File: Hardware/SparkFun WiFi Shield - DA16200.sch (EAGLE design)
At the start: 27 parts, among them J1 CORTEX_JTAG_DEBUG, U1 DA16200MOD-AAC4WA32

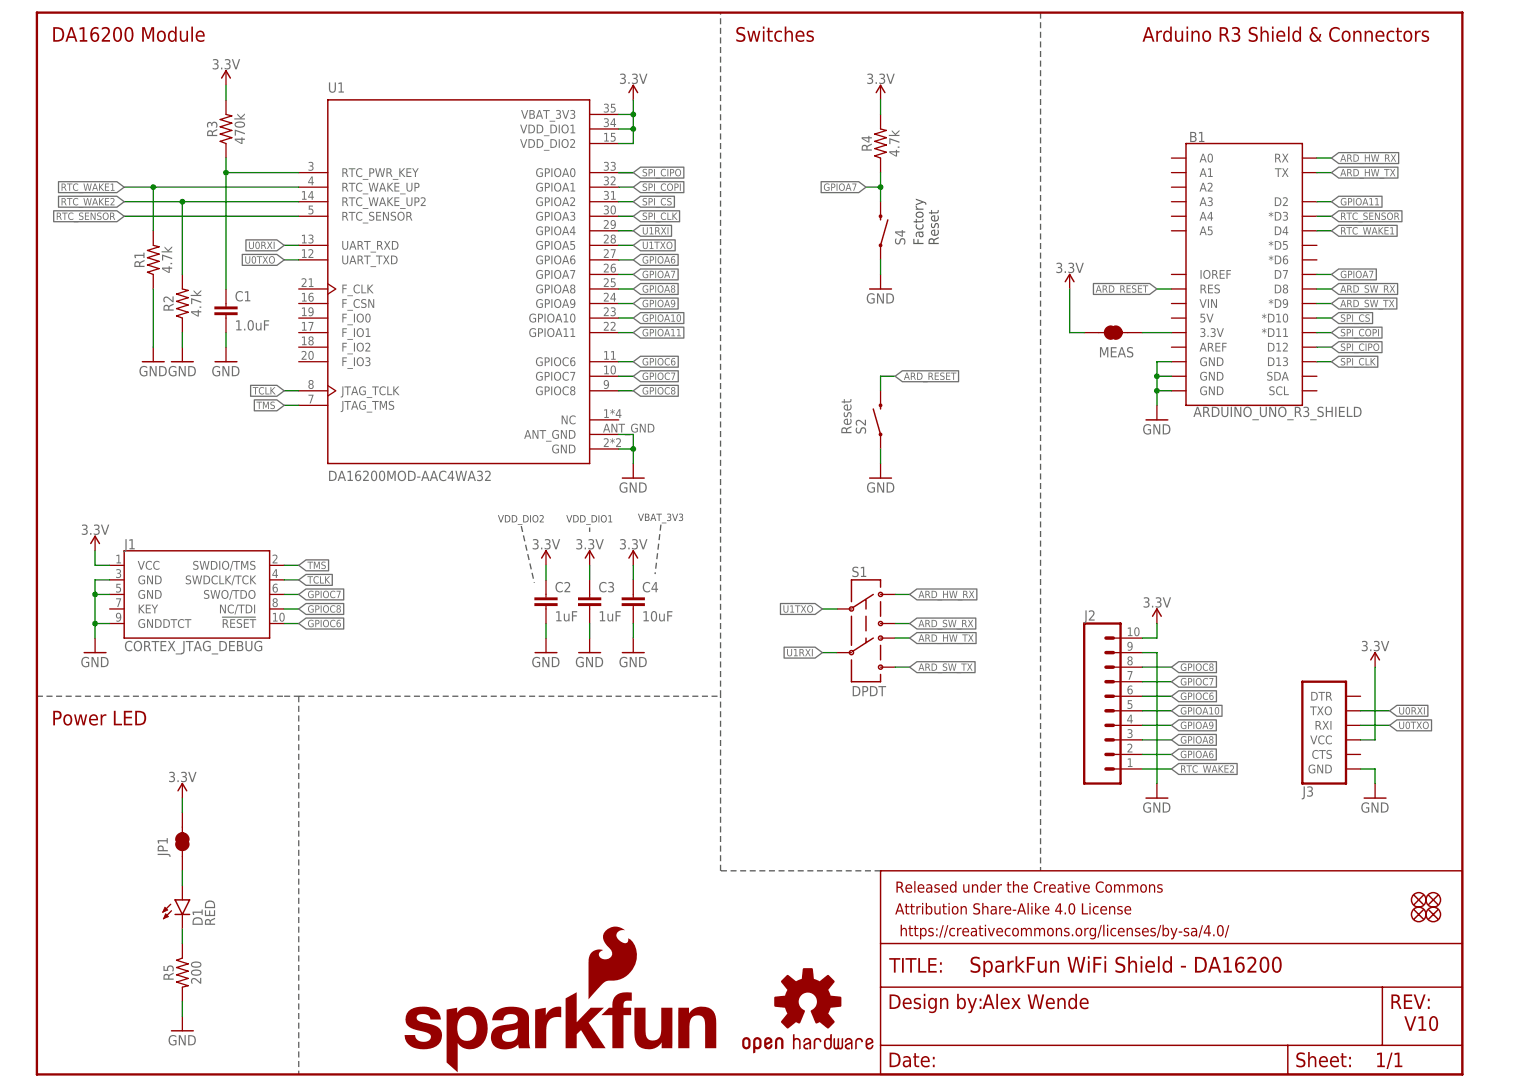
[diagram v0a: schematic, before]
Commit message: V10 Dialog Changes
- GPIOA6 needs 4.7k Pullup
- GPIOA10 - added 2-way jumper for MCU (SPI Interrupt) and Header (PWM)
- GPIOC6,7,8 not needed for JTAG
- Removed RTC Sensor, RTC_WAKE1, RTC_WAKE2
- PCB - Moved VDD trace, enlarged ground connection for RF GND on bottom, added more vias in large ground areas
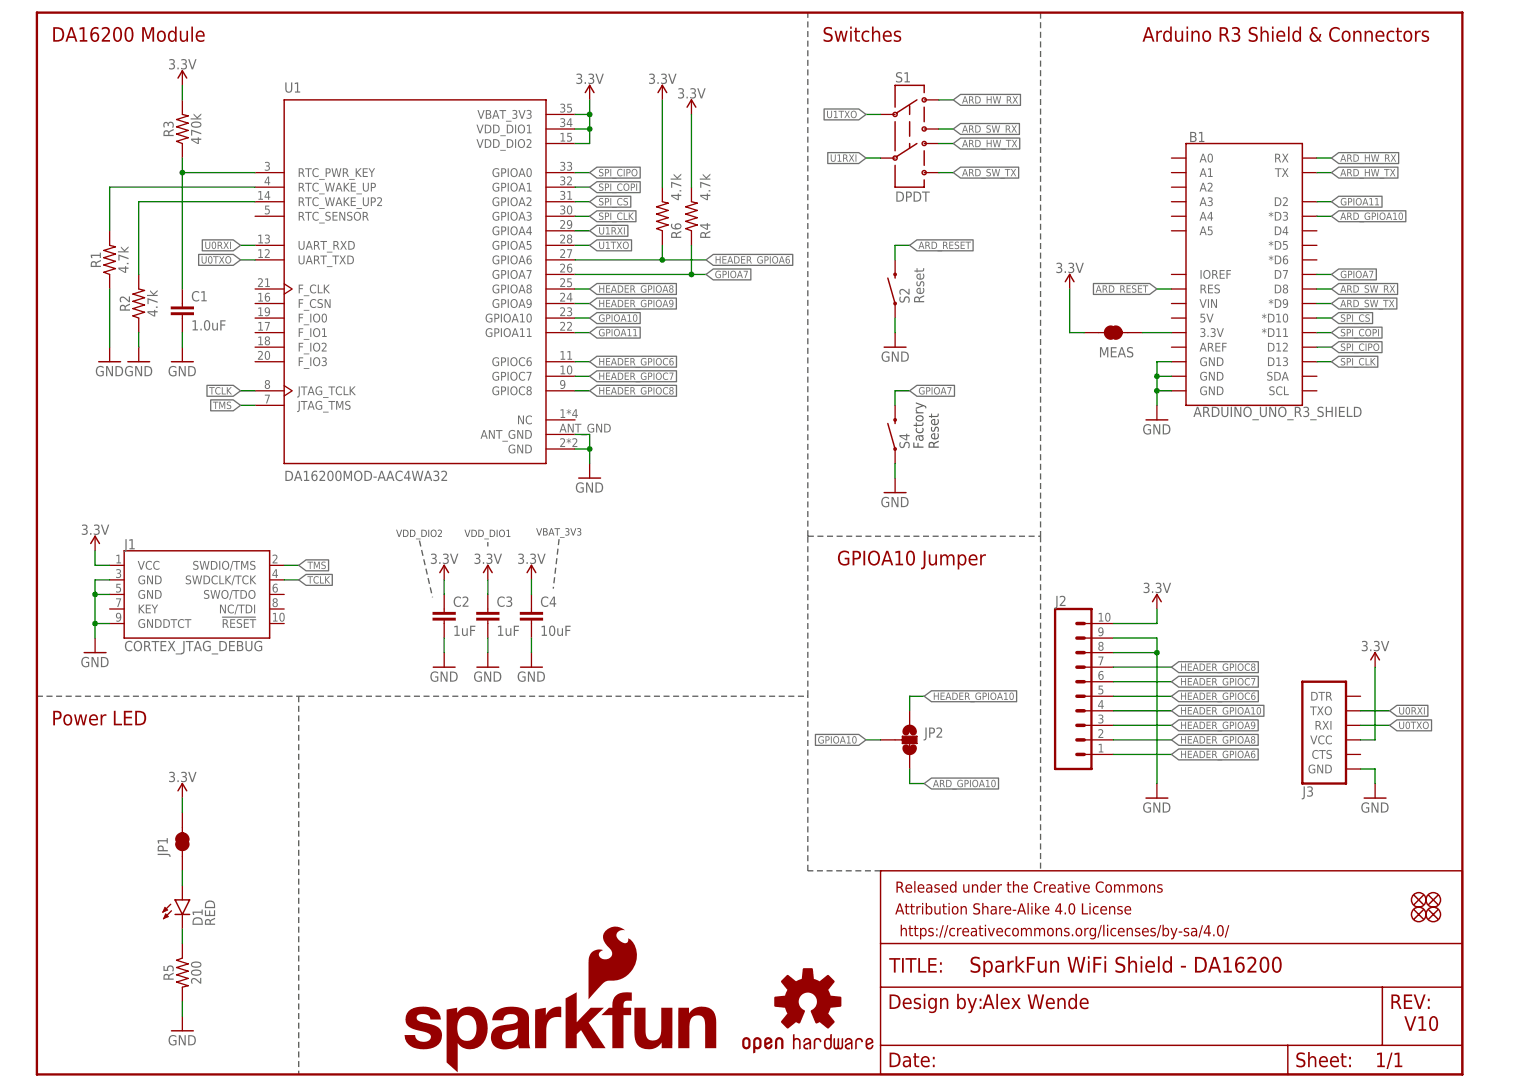
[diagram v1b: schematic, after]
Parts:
- added JP2: JUMPER-SMT_3_1-NC_TRACE_NO-SILK, SparkFun-Jumpers:JUMPER-SMT_3_1-NC_TRACE_NO-SILK
- added R6: 4.7k, SparkFun-Resistors:4.7KOHM-0603-1/10W-1%
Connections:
- removed net GPIOA6: J2.2, U1.GPIOA6
- removed net GPIOA8: J2.3, U1.GPIOA8
- removed net GPIOA9: J2.4, U1.GPIOA9
- removed net GPIOC6: J1.!RESET, J2.6, U1.GPIOC6
- removed net GPIOC7: J1.SWO/TDO, J2.7, U1.GPIOC7
- removed net GPIOC8: J1.NC/TDI, J2.8, U1.GPIOC8
- removed net RTC_SENSOR: B1.*D3, U1.RTC_SENSOR
- removed net RTC_WAKE2: J2.1, R2.2, U1.RTC_WAKE_UP2
- new net ARD_GPIOA10: B1.*D3, JP2.3
- new net HEADER_GPIOA10: J2.4, JP2.1
- new net HEADER_GPIOA6: J2.1, R6.1, U1.GPIOA6
- new net HEADER_GPIOA8: J2.2, U1.GPIOA8
- new net HEADER_GPIOA9: J2.3, U1.GPIOA9
- new net HEADER_GPIOC6: J2.5, U1.GPIOC6
- new net HEADER_GPIOC7: J2.6, U1.GPIOC7
- new net HEADER_GPIOC8: J2.7, U1.GPIOC8
- new net HEADER_RTC_WAKE2: R2.2, U1.RTC_WAKE_UP2
- net 3.3V: now also R6.2
- net GND: now also J2.8
- net GPIOA10: now also JP2.2; no longer J2.5
- net RTC_WAKE1: no longer B1.D4
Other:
- note added: "GPIOA10 Jumper"
- moved on the sheet: C1, C2, C3, C4, J2, R1, R2, R3, R4, S1, S2, S4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

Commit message: Parts Update
Updated library for module, added 470k resistor, updated symbols, added jumper notes
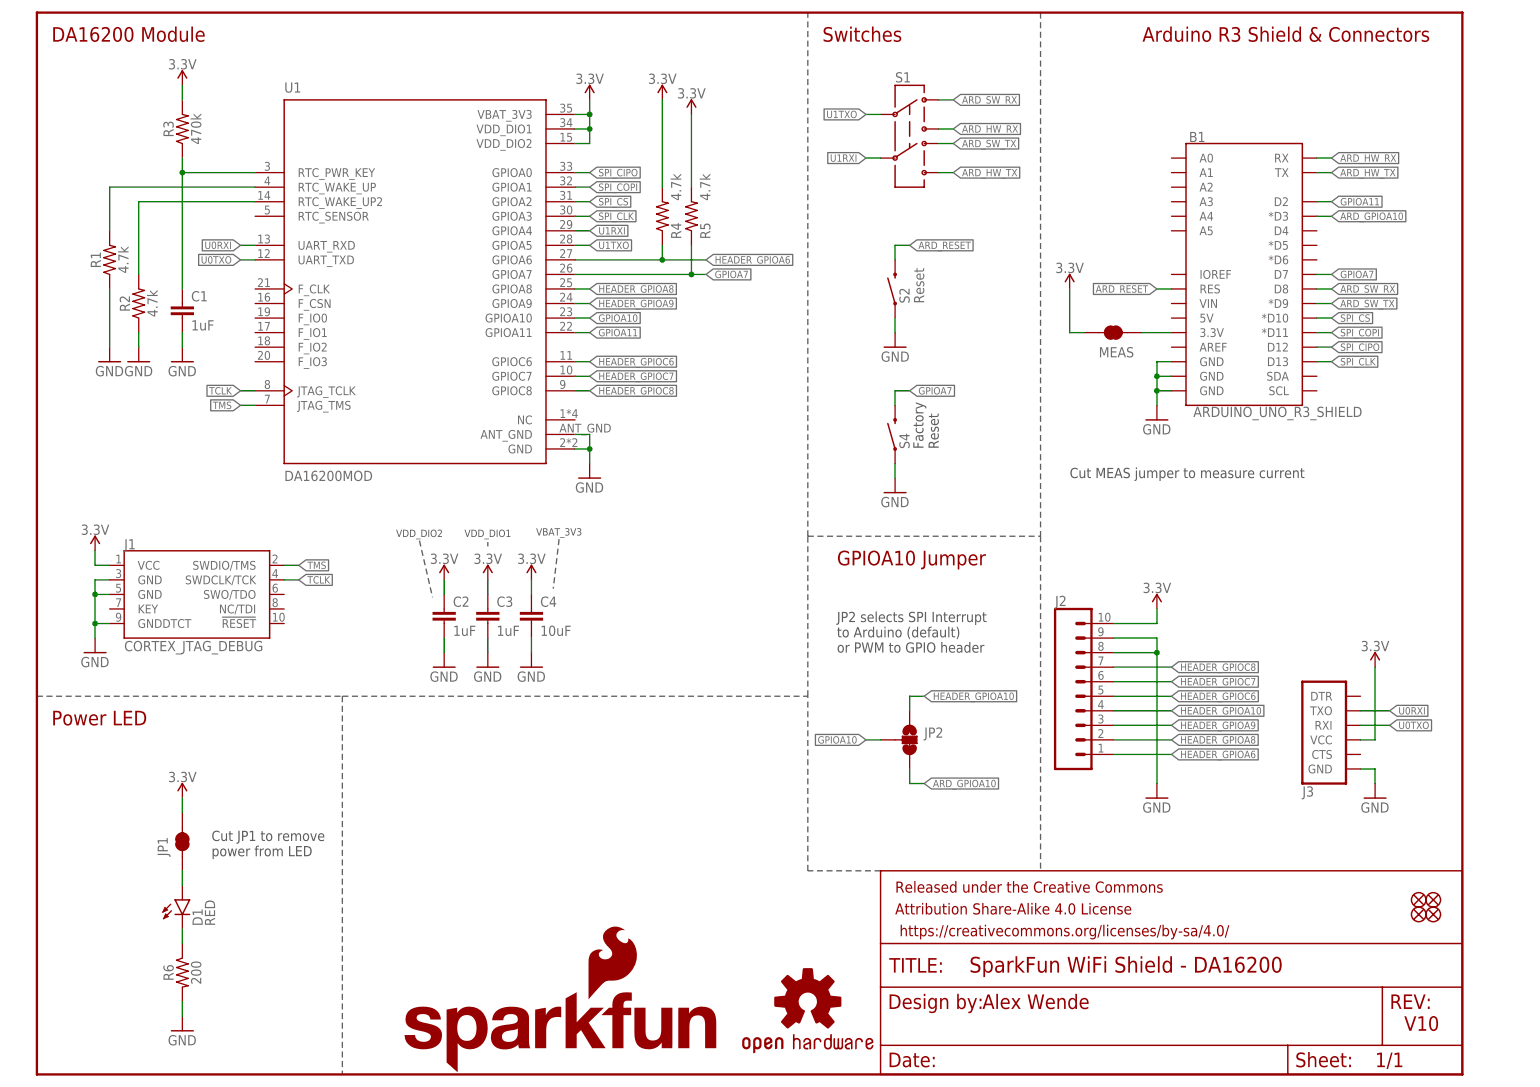
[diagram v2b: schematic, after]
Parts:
- C1: value 1.0uF -> 1uF
- JP2: value JUMPER-SMT_3_1-NC_TRACE_NO-SILK -> JUMPER-SMT_3_1-NC_TRACE_SILK; device SparkFun-Jumpers:JUMPER-SMT_3_1-NC_TRACE_NO-SILK -> SparkFun-Jumpers:JUMPER-SMT_3_1-NC_TRACE_SILK
- R3: device SparkFun-Resistors:453KOHM-0603-1/10W-1% -> SparkFun-Resistors:470KOHM
- R5: value 200 -> 4.7k; device SparkFun-Resistors:200OHM-0603-1/10W-1% -> SparkFun-Resistors:4.7KOHM-0603-1/10W-1%
- R6: value 4.7k -> 200; device SparkFun-Resistors:4.7KOHM-0603-1/10W-1% -> SparkFun-Resistors:200OHM-0603-1/10W-1%
- S1: device SparkFun-Electromechanical:SWITCH-DPDTAYZ0202 -> SparkFun-Switches:SWITCH-DPDT-SMD-AYZ0202
- U1: value DA16200MOD-AAC4WA32 -> DA16200MOD; device DA16200MOD-AAC4WA32:DA16200MOD-AAC4WA32 -> DA16200MOD:DA16200MOD-AAC4WA32
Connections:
- net 3.3V: now also R5.2; no longer R6.2
- net GND: now also R6.2; no longer R5.2
- net GPIOA7: now also R5.1; no longer R4.1
- net HEADER_GPIOA6: now also R4.1; no longer R6.1
- net N$5: now also R6.1; no longer R5.1
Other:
- note added: "Cut JP1 to remove power from LED"
- note added: "Cut MEAS jumper to measure current"
- note added: "JP2 selects SPI Interrupt to Arduino (default) or PWM to GPIO header"
- moved on the sheet: R4, R5, R6

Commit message: Added I2C
Added I2C connections, Qwiic connector, pullup resistors, and jumper
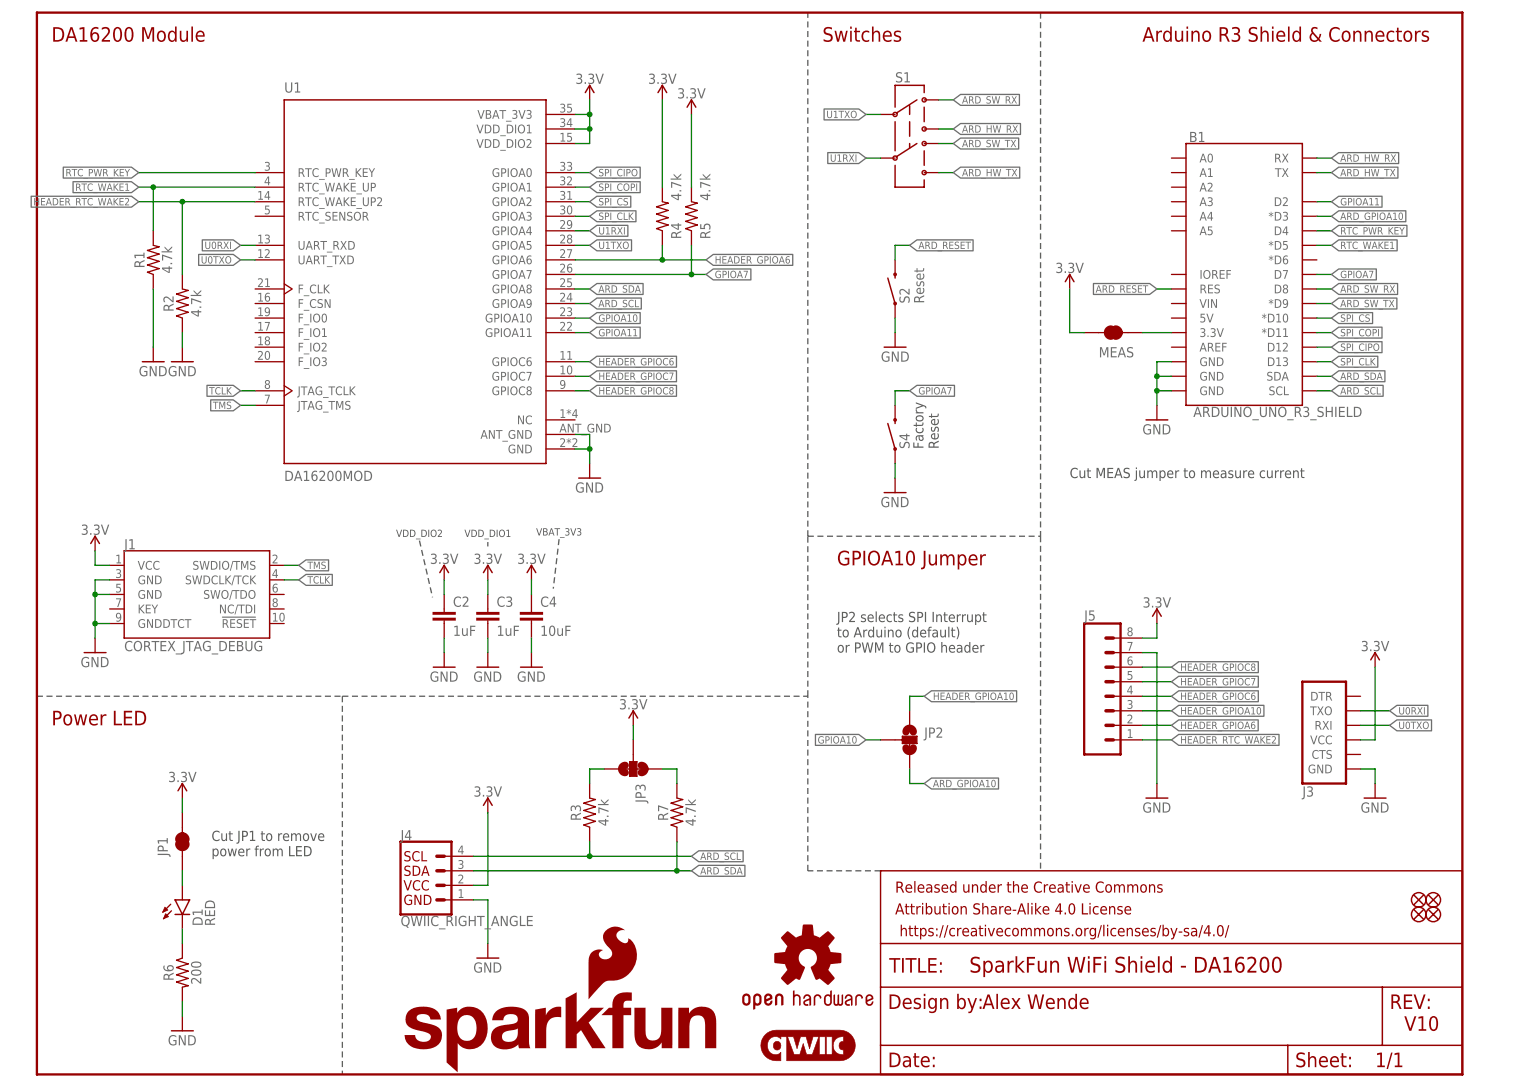
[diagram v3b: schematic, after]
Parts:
- removed C1: 1uF, SparkFun-Capacitors:1.0UF-0603-16V-10%
- removed J2: (no value), SparkFun-Connectors:CONN_10NO_SILK_PTH_FEMALE
- added J4: QWIIC_RIGHT_ANGLE, SparkFun-Connectors:QWIIC_CONNECTORJS-1MM
- added J5: (no value), SparkFun-Connectors:CONN_08NO_SILK_DNP
- added JP3: JUMPER-SMT_3_2-NC_TRACE_SILK, SparkFun-Jumpers:JUMPER-SMT_3_2-NC_TRACE_SILK
- added LOGO4: QWIIC_LOGO_5MM, SparkFun-Aesthetics:QWIIC_LOGO_5MM
- added R7: 4.7k, SparkFun-Resistors:4.7KOHM-0603-1/10W-1%
- R3: value 470k -> 4.7k; device SparkFun-Resistors:470KOHM -> SparkFun-Resistors:4.7KOHM-0603-1/10W-1%
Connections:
- removed net HEADER_GPIOA8: J2.2, U1.GPIOA8
- removed net HEADER_GPIOA9: J2.3, U1.GPIOA9
- new net ARD_SCL: B1.SCL, J4.4, R3.1, U1.GPIOA9
- new net ARD_SDA: B1.SDA, J4.3, R7.1, U1.GPIOA8
- new net N$3: JP3.3, R3.2
- new net N$4: JP3.1, R7.2
- net 3.3V: now also J4.2, J5.8, JP3.2; no longer J2.10, R3.2
- net GND: now also J4.1, J5.7; no longer C1.2, J2.8, J2.9
- net HEADER_GPIOA10: now also J5.3; no longer J2.4
- net HEADER_GPIOA6: now also J5.2; no longer J2.1
- net HEADER_GPIOC6: now also J5.4; no longer J2.5
- net HEADER_GPIOC7: now also J5.5; no longer J2.6
- net HEADER_GPIOC8: now also J5.6; no longer J2.7
- net HEADER_RTC_WAKE2: now also J5.1
- net RTC_PWR_KEY: now also B1.D4; no longer C1.1, R3.1
- net RTC_WAKE1: now also B1.*D5
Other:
- moved on the sheet: R1, R2, R3

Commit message: V10 Design Review Changes
Updated label positions, added notes to sch
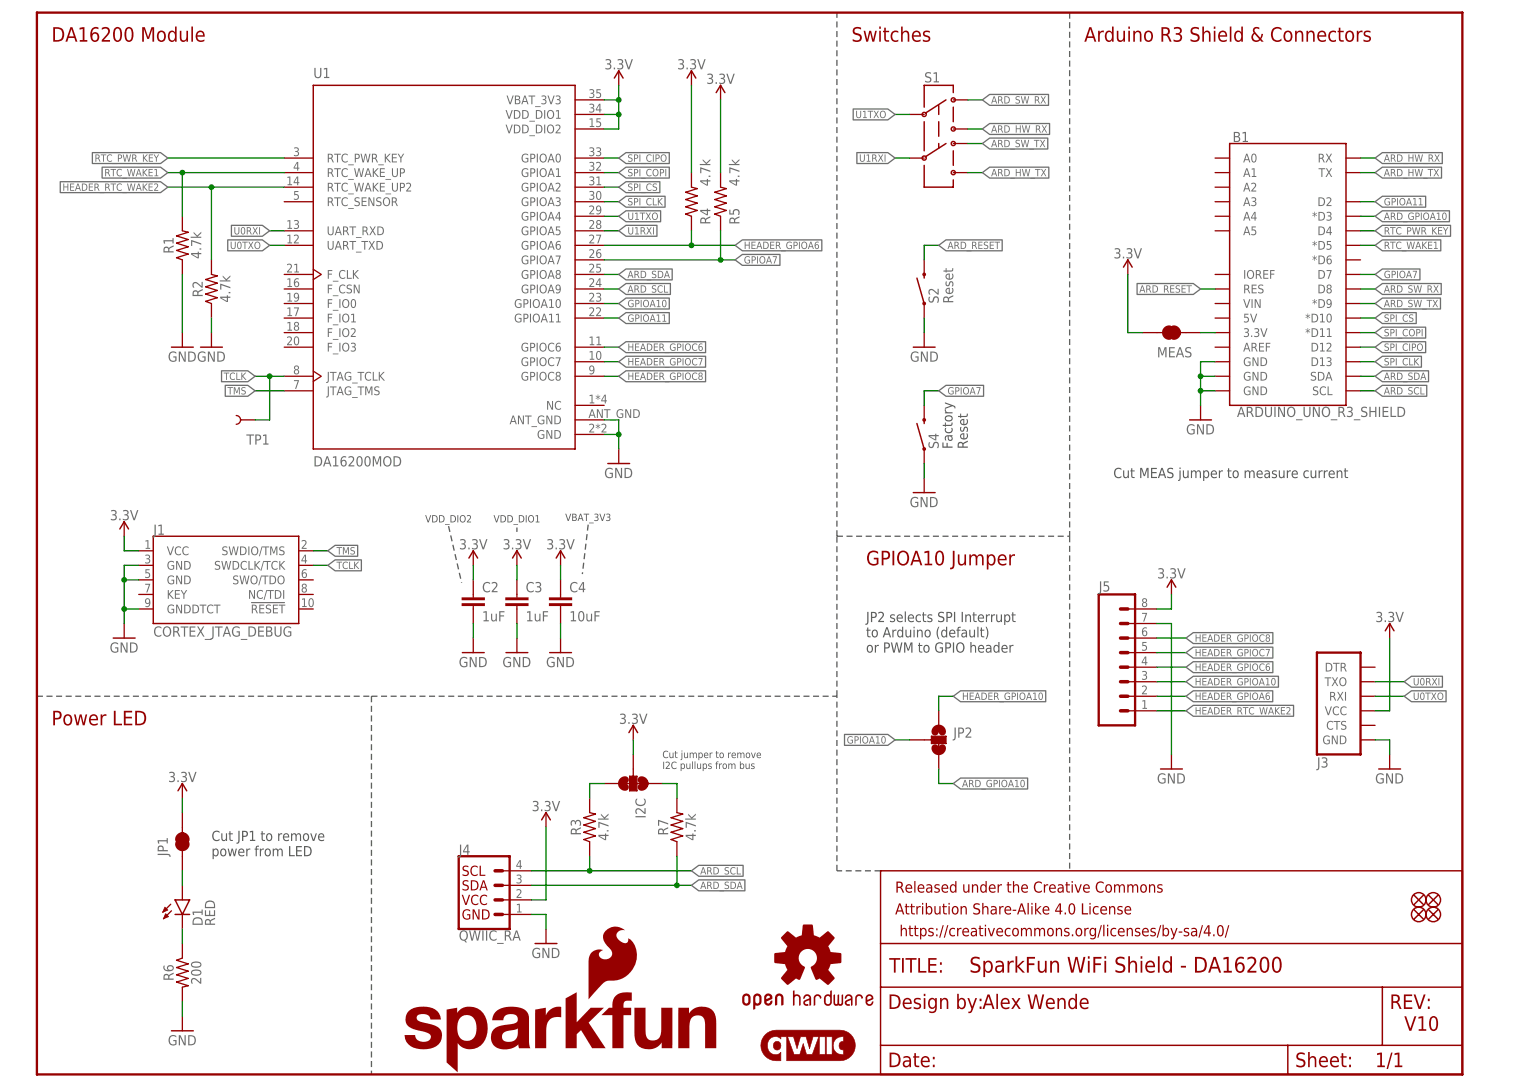
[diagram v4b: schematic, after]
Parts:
- removed JP3: JUMPER-SMT_3_2-NC_TRACE_SILK, SparkFun-Jumpers:JUMPER-SMT_3_2-NC_TRACE_SILK
- added I2C: JUMPER-SMT_3_2-NC_TRACE_SILK, SparkFun-Jumpers:JUMPER-SMT_3_2-NC_TRACE_SILK
- added TP1: TEST-POINT3, SparkFun-Connectors:TEST-POINT3
- J4: value QWIIC_RIGHT_ANGLE -> QWIIC_RA
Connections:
- net 3.3V: now also I2C.2; no longer JP3.2
- net N$3: now also I2C.3; no longer JP3.3
- net N$4: now also I2C.1; no longer JP3.1
- net TCLK: now also TP1.1
- net U1RXI: now also U1.GPIOA5; no longer U1.GPIOA4
- net U1TXO: now also U1.GPIOA4; no longer U1.GPIOA5
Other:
- note added: "Cut jumper to remove I2C pullups from bus"
- moved on the sheet: B1, C2, C3, C4, J1, J3, J4, J5, JP2, MEAS, R1, R2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
